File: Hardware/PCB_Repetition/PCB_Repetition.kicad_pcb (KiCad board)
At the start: 4 copper layers, 389.9 x 88.9 mm, 98 parts, among them J1 Conn_01x03, J10 XLR3, J11 XLR3, J12 XLR3, J13 XLR3, J14 XLR3, J15 XLR3, J16 XLR3, J17 XLR3, J18 XLR3, J19 Conn_01x04, J2 XLR3, J20 Conn_01x04, J21 Conn_01x04, J3 XLR3, J4 Conn_01x03, J5 Conn_01x03, J6 Conn_01x03, J7 XLR3, J8 XLR3, J9 XLR3, Q1 SQ2310ES-T1_BE3, Q2 SQ2310ES-T1_BE3, Q3 SQ2310ES-T1_BE3, Q4 SQ2310ES-T1_BE3, Q5 SQ2310ES-T1_BE3, Q6 SQ2310ES-T1_BE3, SW1 SW_SPST, SW2 SW_SPST, SW3 SW_DIP_x02, SW4 SW_DIP_x02, SW5 SW_DIP_x02, SW6 SW_DIP_x02, SW7 SW_DIP_x02, SW8 SW_DIP_x02, SW9 SW_DIP_x02, U2 ZXBM5210-SP, U4 PCF8575DBR

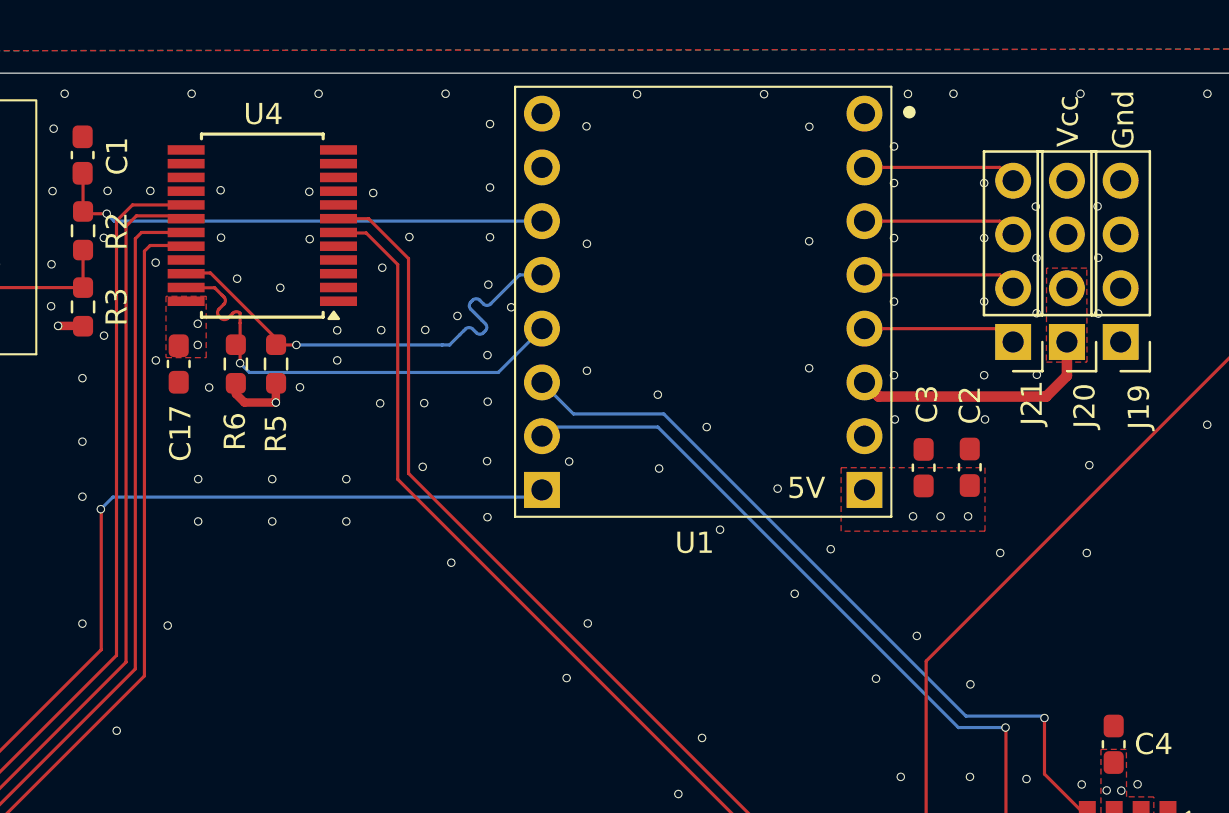
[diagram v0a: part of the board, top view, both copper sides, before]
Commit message: correction des pull-up sur SDA/SCL, finalisation du code esp32 Google_Calendar pour que la reconnexion (sur google device)se fasse automatiquement après reboot
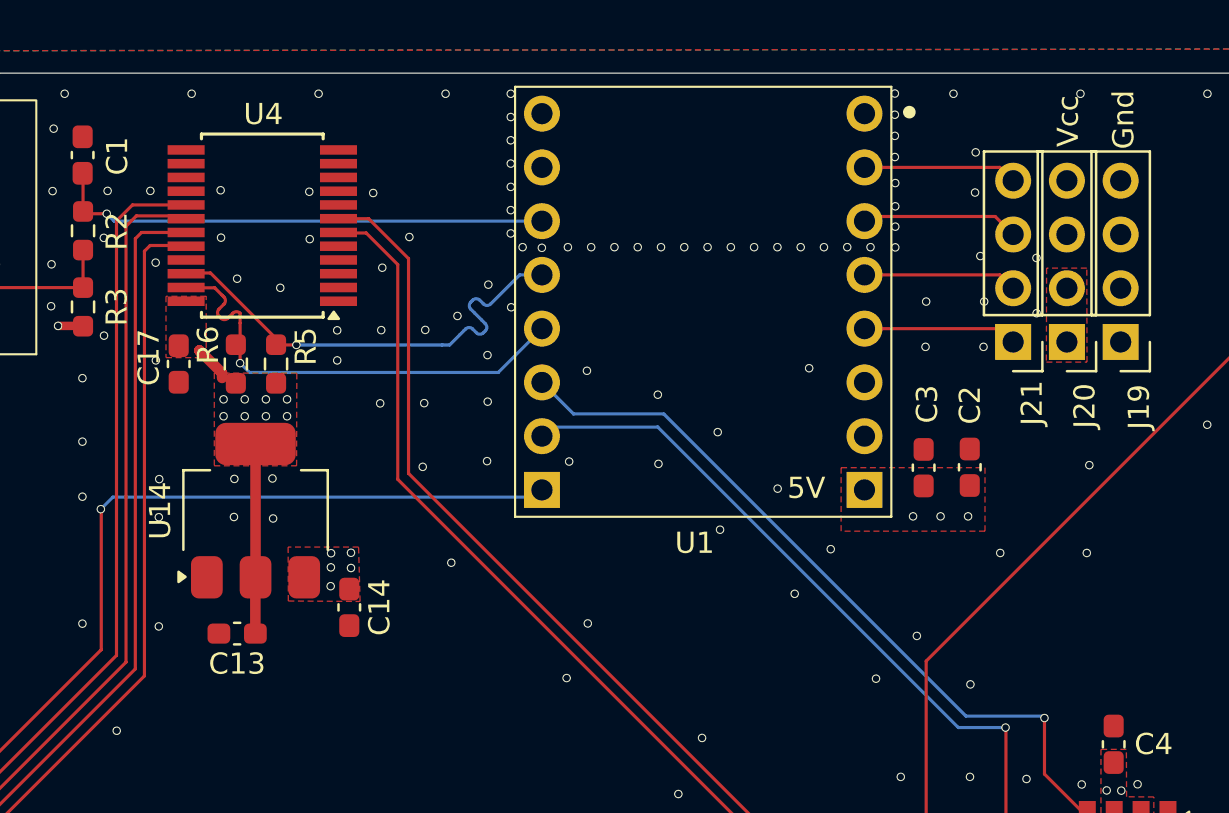
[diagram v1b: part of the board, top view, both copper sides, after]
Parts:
- added C13: 22u, Capacitor_SMD:C_0603_1608Metric_Pad1.08x0.95mm_HandSolder, F.Cu at (125.5, 174.9)
- added C14: 10u, Capacitor_SMD:C_0603_1608Metric_Pad1.08x0.95mm_HandSolder, F.Cu at (130.8, 173.7)
- added U14: AZ1117-3.3, Package_TO_SOT_SMD:SOT-223-3_TabPin2, F.Cu at (126.3, 169.1)
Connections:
- C17 pad 2: +5V -> +3.3V
- J20 pad 1: +3.3V -> +5V
- J20 pad 2: +3.3V -> +5V
- J20 pad 3: +5V -> +3.3V
- J20 pad 4: +5V -> +3.3V
- R5 pad 1: +5V -> +3.3V
- R6 pad 1: +5V -> +3.3V
- U1 pad 6: +3.3V -> unconnected-(U1-3.3V-Pad6)
- U4 pad 24: +5V -> +3.3V
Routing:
- net +3.3V: track 11.8 -> 57.9 mm, vias 0 -> 8
- net +5V: track 24.3 -> 20.9 mm, vias 22 -> 24
- net GND: vias 761 -> 770
- added copper zone on In2.Cu, net +3.3V
